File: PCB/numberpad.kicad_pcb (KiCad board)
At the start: 2 copper layers, 97 x 124.9 mm, 72 parts, among them J1 Light_Sensor, J2 Rotary_Encoder, J3 Screen_Connector, J4 FingerPrint_UART, J5 USB_A, J6 Programmer, J7 USB_C_TO_PC, SW0 0, SW1 ., SW10 8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

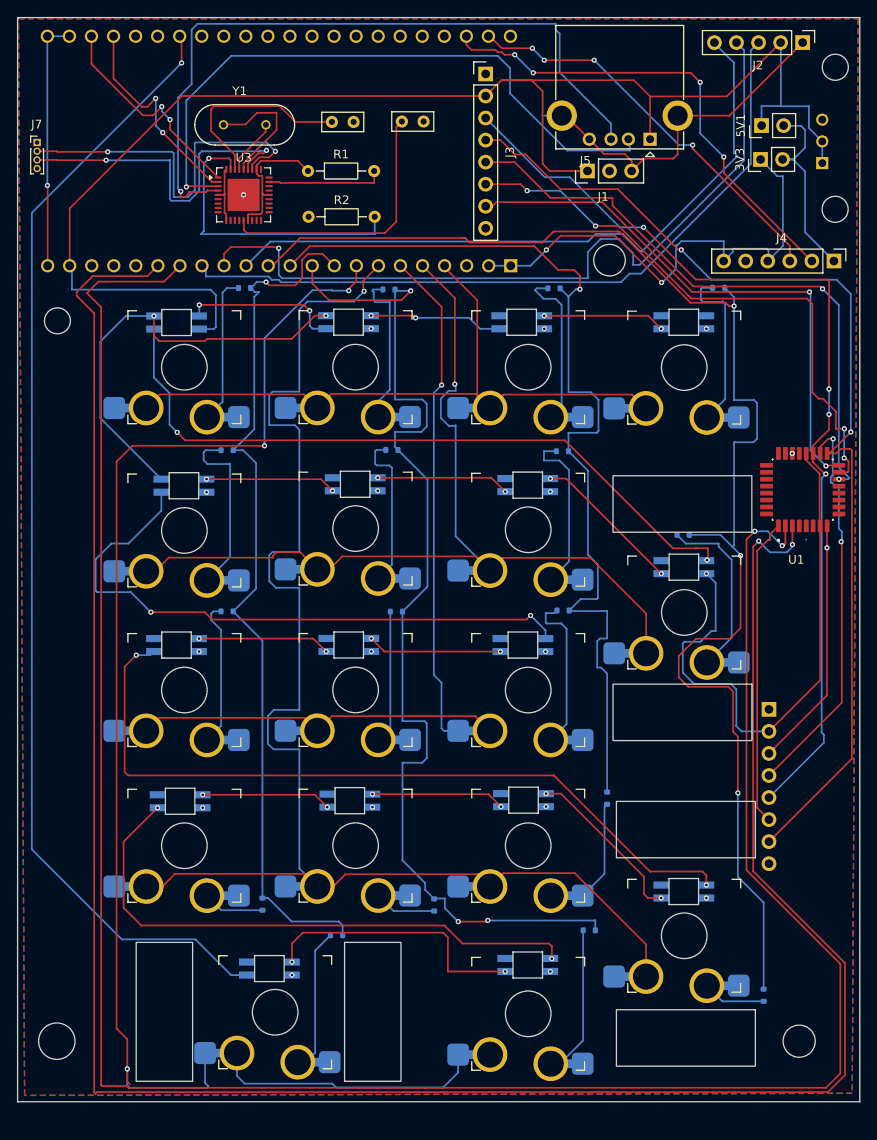
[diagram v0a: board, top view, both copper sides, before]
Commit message: Personalisation is now a thing
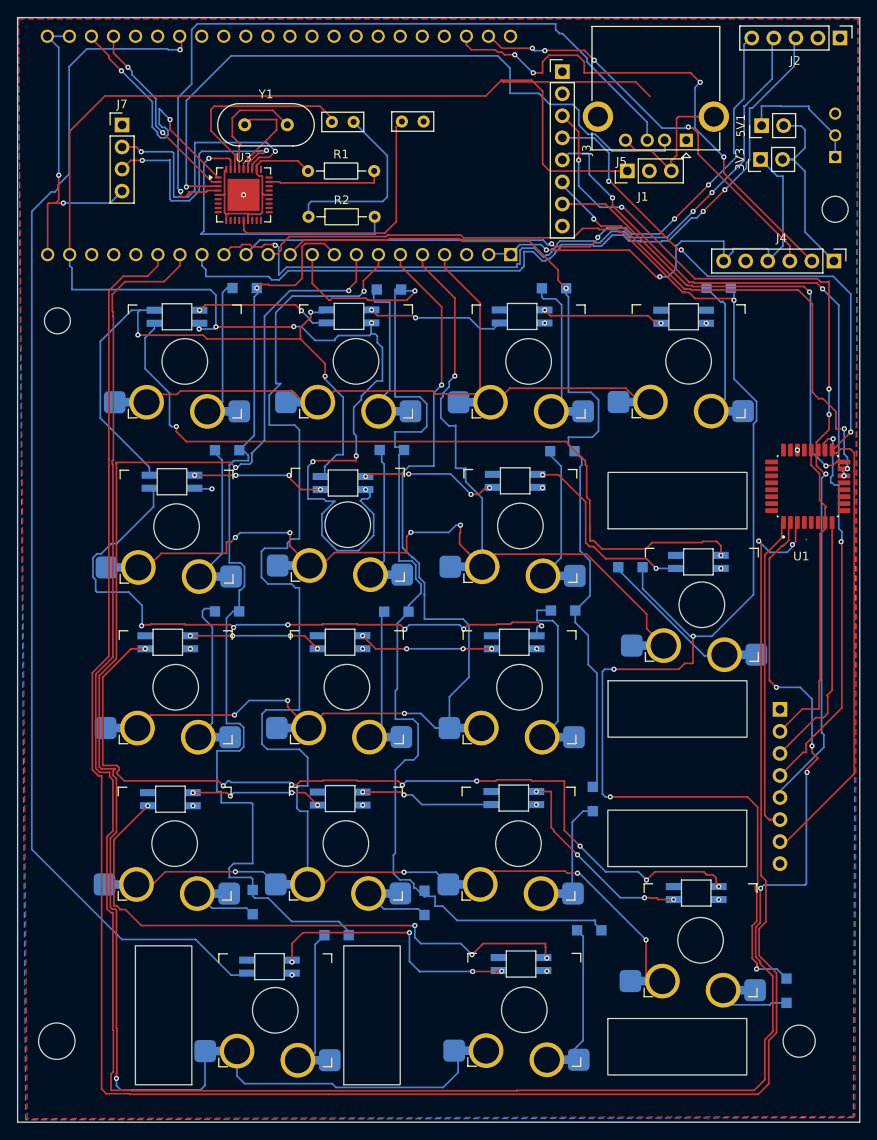
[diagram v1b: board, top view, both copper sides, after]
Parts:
- D0, D1, D10, D11, D12, D13, D14, D15, D16, D2, D3, D4, D5, D6, D7, D8, D9: footprint Diode_SMD:D_SOD-523 -> Diode_SMD:Nexperia_CFP3_SOD-123W
- J7: footprint Connector_PinHeader_1.00mm:PinHeader_1x04_P1.00mm_Vertical -> Connector_PinHeader_2.54mm:PinHeader_1x04_P2.54mm_Vertical
- Y1: footprint footprints:XTAL_HC49P488W43L1150T466H350 -> Crystal:Crystal_HC18-U_Vertical
- moved J7 9.99 mm to (52.2, 53.2)
- moved J3 8.83 mm to (102.9, 47.1)
- moved D12 7.12 mm to (110.8, 104.2)
- moved J1 4.58 mm to (110.4, 58.5)
- moved J2 4.33 mm to (134.9, 43.2)
- moved J5 4.17 mm to (117.2, 55.0)
- moved REF** 3.06 mm to (118.0, 108.5), turned to -90 degrees
- moved REF** 2.80 mm to (118.0, 147.4), turned to -90 degrees
- moved D5 2.69 mm to (128.8, 152.9)
- moved SW12 2.21 mm to (119.0, 108.5)
- moved SW5 1.95 mm to (118.8, 147.1)
- moved D29 1.78 mm to (118.6, 103.6)
- moved D4 1.65 mm to (106.4, 130.9)
- moved S1 1.65 mm to (134.4, 54.4)
- moved D28 1.53 mm to (97.5, 94.2)
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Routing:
- net GND: track 172.9 -> 200.6 mm
- net C3: track 163.4 -> 185.1 mm, vias 3 -> 5
- net 5V: track 235.4 -> 256.8 mm, vias 16 -> 21
- net C0: track 101.5 -> 116.0 mm
- net TX: track 264.3 -> 251.2 mm
- net C2: track 113.5 -> 102.2 mm
- net SCREEN_DC: track 66.4 -> 55.9 mm, vias 4 -> 3
- net R1_LED: track 89.3 -> 99.8 mm, vias 2 -> 8
- net R1: track 109.3 -> 119.2 mm, vias 1 -> 5
- net D-: track 42.9 -> 33.3 mm
- net D+: track 39.4 -> 30.0 mm
- net R3_LED: track 81.1 -> 89.8 mm
- net SCREEN_RST: track 69.7 -> 61.2 mm, vias 2 -> 3
- net SCREEN_CS: track 64.2 -> 56.0 mm
- net PB3: track 121.2 -> 113.4 mm, vias 2 -> 3
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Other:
- board size 97 x 124.9 mm -> 97 x 127.2 mm

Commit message: fix
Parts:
- added SW17: SW_Push, Button_Switch_THT:SW_TH_Tactile_Omron_B3F-100x, B.Cu at (117.0, 44.1)
- U3: footprint Package_DFN_QFN:QFN-36-1EP_6x6mm_P0.5mm_EP3.7x3.7mm -> footprints:SQFN36_6X6_MCH
- Y1: footprint Crystal:Crystal_HC18-U_Vertical -> Crystal:Crystal_HC49-U_Vertical
- moved D17 1.38 mm to (69.1, 148.8)
- moved SW0 1.38 mm to (69.8, 153.8)
- moved SW12 1.04 mm to (118.0, 108.3)
- moved SW5 1.00 mm to (117.8, 147.1)
- moved D29 0.92 mm to (117.7, 103.3)
- moved D22 0.63 mm to (117.7, 141.6)
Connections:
- U2 pad J1_3: RST -> Net-(U2-RST)
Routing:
- net 5V: track 256.8 -> 148.3 mm
- net Net-(U2-RST): track 0.00 -> 47.8 mm, vias 0 -> 3
- net R2: track 107.3 -> 130.4 mm
- net R1: track 119.2 -> 134.0 mm
- net R0: track 84.7 -> 99.4 mm
- net R3: track 168.6 -> 182.0 mm
- net +3.3V: track 25.2 -> 37.8 mm, vias 0 -> 5
- net R4: track 172.0 -> 183.4 mm
- net GND: track 200.6 -> 207.6 mm
- net Net-(U3-XTALOUT): track 11.2 -> 5.24 mm
- net R2_LED: track 73.1 -> 77.3 mm
- net Net-(D12-A): track 14.7 -> 18.6 mm
- net Net-(D3-A): track 7.48 -> 11.2 mm
- net Net-(D8-A): track 19.2 -> 22.9 mm
- net Net-(D10-A): track 15.5 -> 19.1 mm
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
